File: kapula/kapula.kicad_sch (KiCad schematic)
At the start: 157 parts, among them J1 Conn_02x10_Odd_Even, J12 U.FL, J13 U.FL, J3 Conn_02x10_Odd_Even, J4 Conn_ARM_JTAG_SWD_10, J5 U.FL, J9 U.FL, Q1 AO3401A, Q1 BSS84, Q2 AO3401A, Q3 AO3400A, Q5 AO3400A, Q6 AO3400A, T1 BW21S7511A01TF, T2 BW21S7511A01TF, T3 BW21S7511A01TF, T4 BW21S7511A01TF, U1 XC6206P332MR, U2 TP4054, U3 DW01+G, U5 EFR32FG14P233F256GM48-B, U6 XA213-G4J, X1 DSB221SDN, Y1 32768 Hz

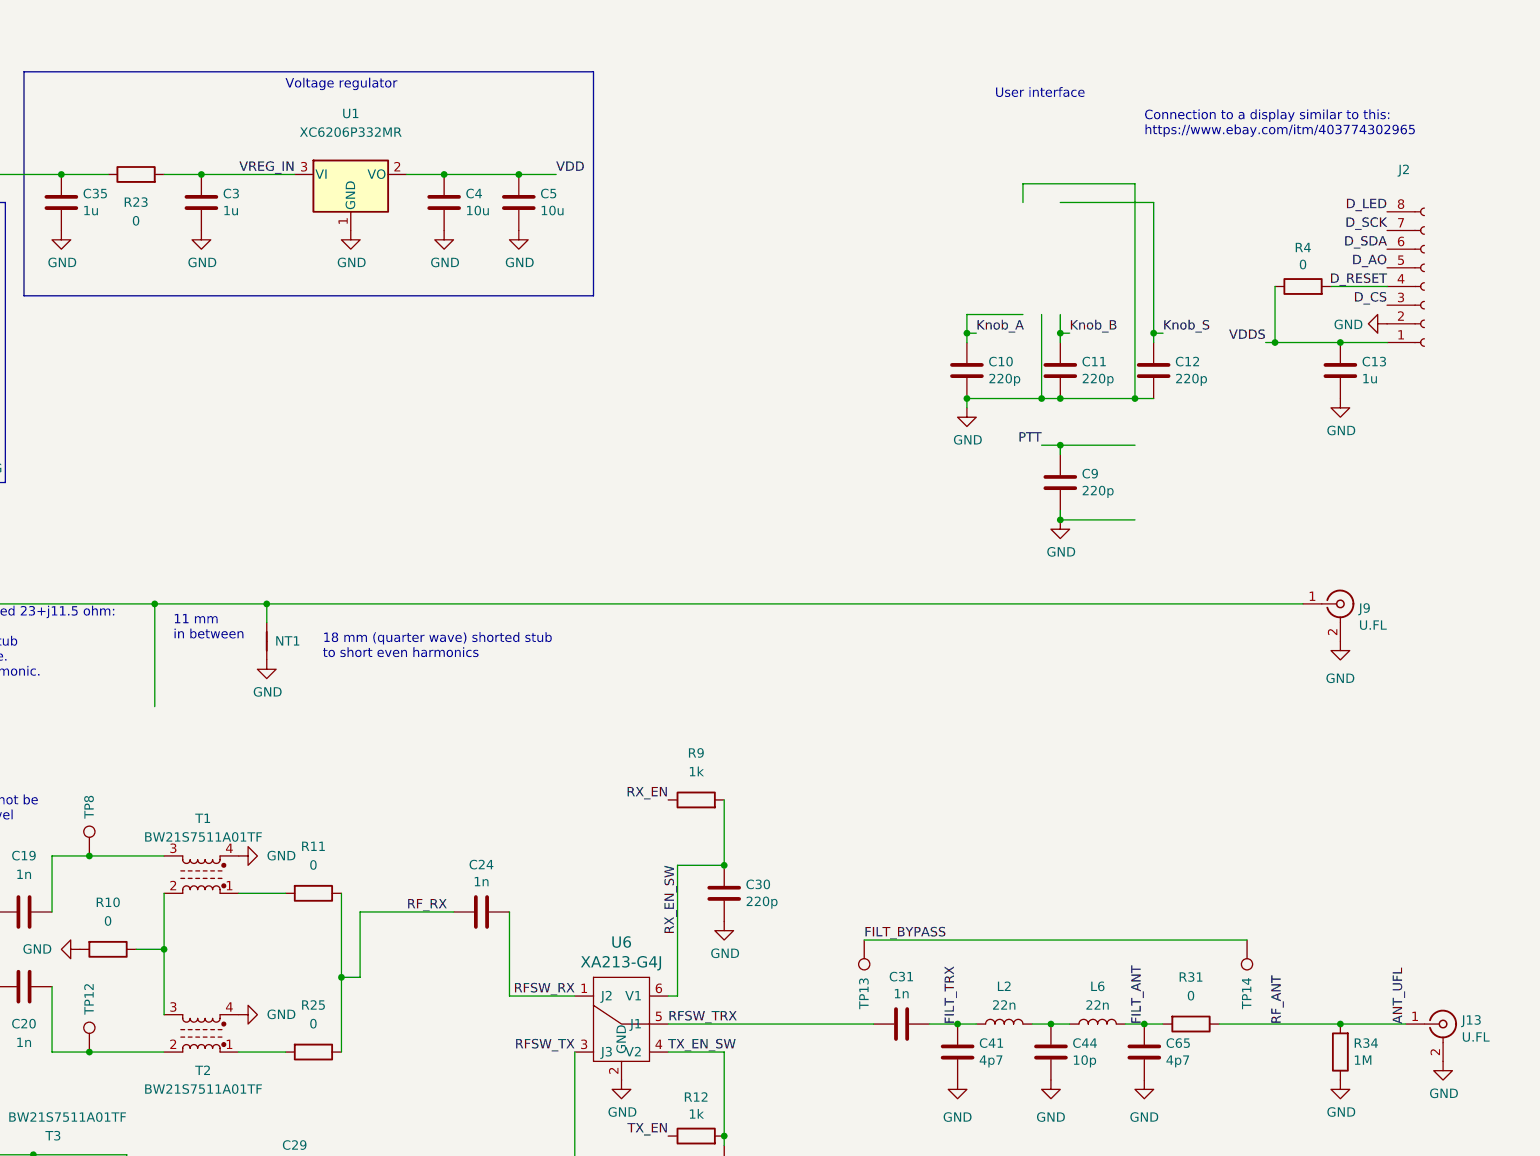
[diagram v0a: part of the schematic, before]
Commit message: PCB: Fix ERC errors
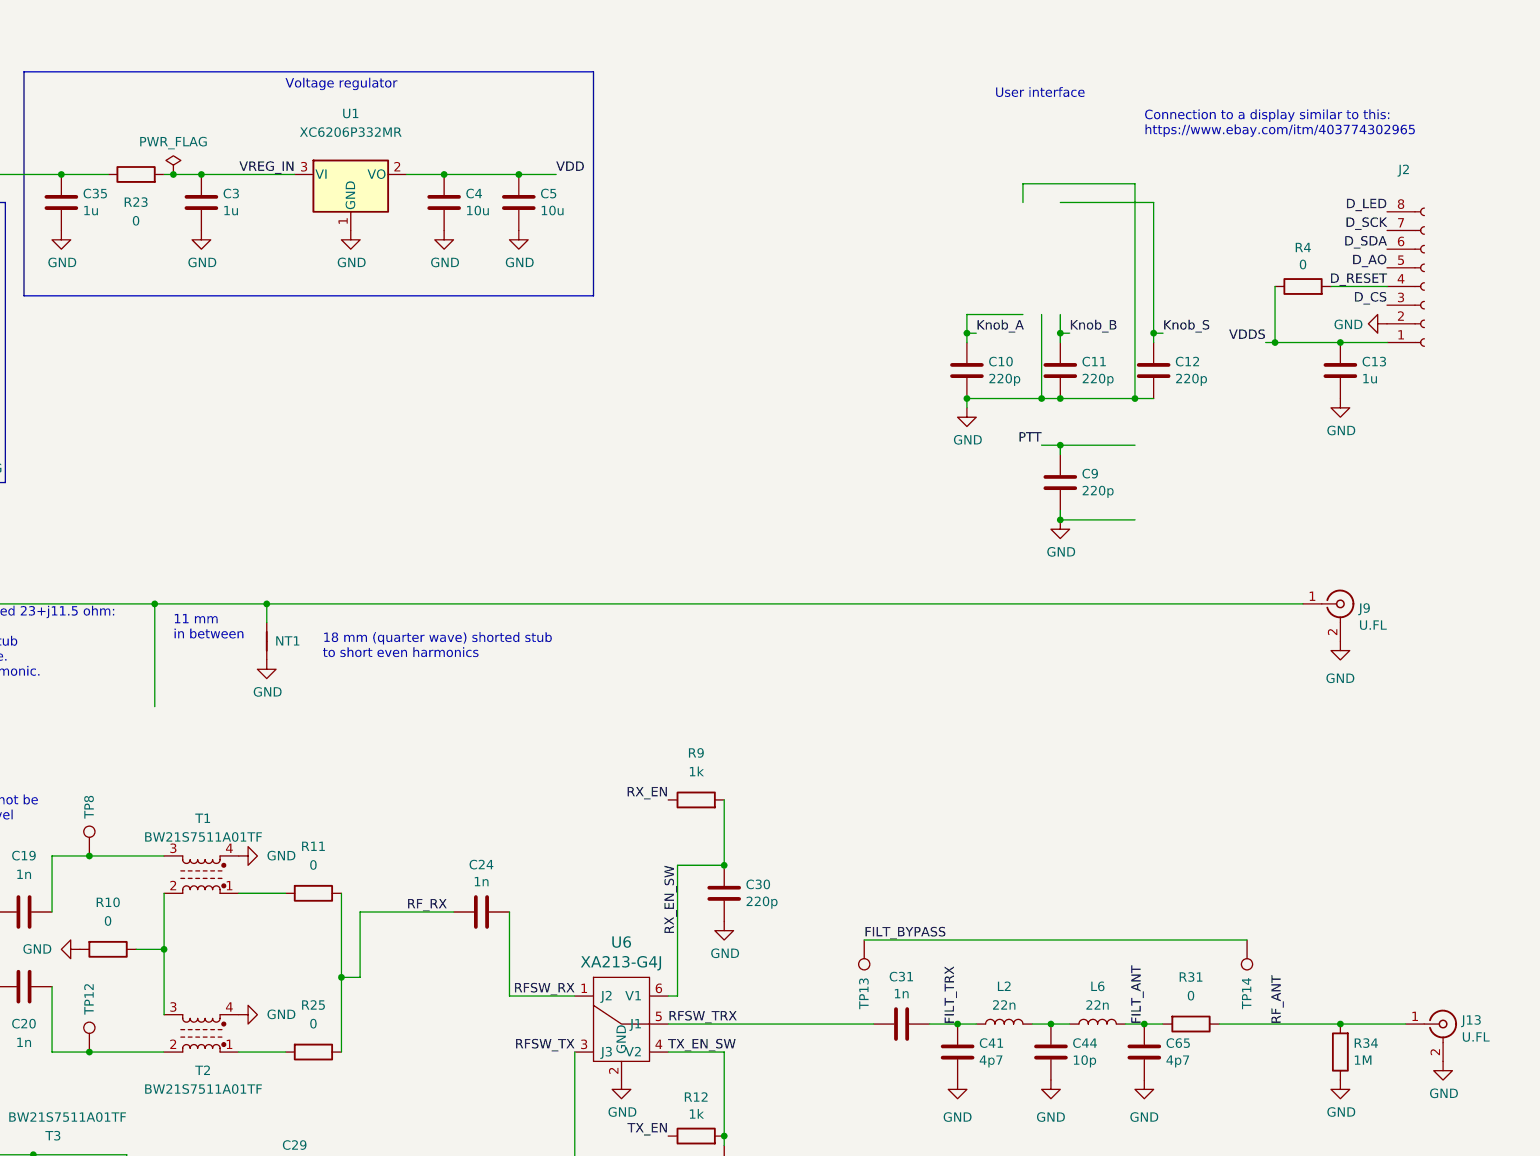
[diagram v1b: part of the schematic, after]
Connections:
- net ANT_UFL renamed RF_ANT
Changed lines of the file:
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@@
   (junction (at 219.71 261.62) (diameter 0) (color 0 0 0 0)
   )
+  (junction (at 232.41 26.67) (diameter 0) (color 0 0 0 0)
+  )
   (junction (at 53.34 119.38) (diameter 0) (color 0 0 0 0)
   )
@@
     (stroke (width 0) (type default))
   )
+  (wire (pts (xy 232.41 26.67) (xy 236.22 26.67))
+    (stroke (width 0) (type default))
+  )
   (polyline (pts (xy 298.45 215.9) (xy 298.45 280.67))
     (stroke (width 0) (type default))
@@
     (stroke (width 0) (type default))
   )
-  (wire (pts (xy 231.14 26.67) (xy 236.22 26.67))
+  (wire (pts (xy 231.14 26.67) (xy 232.41 26.67))
     (stroke (width 0) (type default))
   )
@@
     (effects (font (size 1.27 1.27)) (justify right bottom))
   )
-  (label "ANT_UFL" (at 400.05 142.24 90) (fields_autoplaced)
-    (effects (font (size 1.27 1.27)) (justify left bottom))
-  )
   (label "Knob_S" (at 328.93 177.8 180) (fields_autoplaced)
     (effects (font (size 1.27 1.27)) (justify right bottom))
@@
         )
       )
+    )
+  )
+  (symbol (lib_id "power:PWR_FLAG") (at 232.41 26.67 0) (unit 1)
+    (in_bom yes) (on_board yes) (dnp no)
+    (property "Reference" "#FLG09" (at 232.41 24.765 0)
+      (effects (font (size 1.27 1.27)) hide)
+    )
+    (property "Value" "PWR_FLAG" (at 232.41 22.2504 0)
+      (effects (font (size 1.27 1.27)))
+    )
+    (property "Footprint" "" (at 232.41 26.67 0)
+      (effects (font (size 1.27 1.27)) hide)
+    )
+    (property "Datasheet" "~" (at 232.41 26.67 0)
+      (effects (font (size 1.27 1.27)) hide)
+    )
+    (pin "1")
+    (instances
+      (project "kapula"
+        (path "/f2315993-072e-45c9-8c85-e79c6d40aba4"
+          (reference "#FLG09") (unit 1)
+        )
+      )

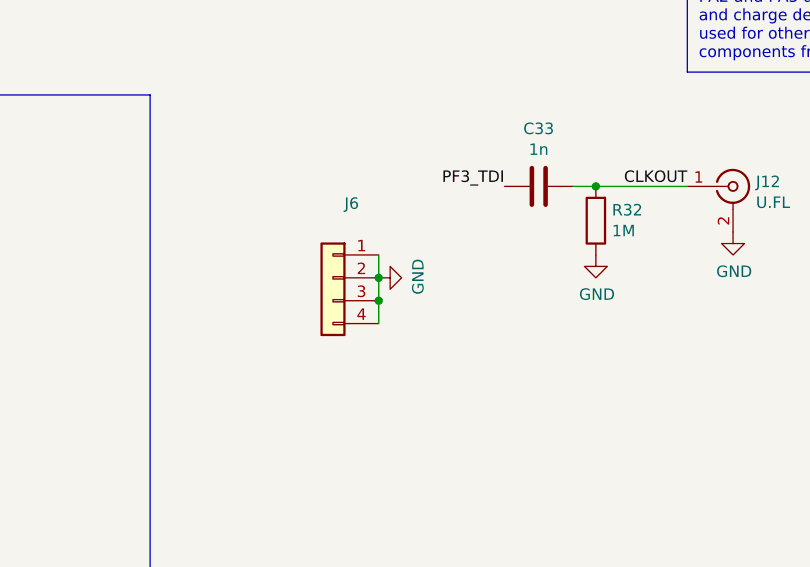
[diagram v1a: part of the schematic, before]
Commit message: PCB: Add 0-ohm resistors for extra ground header
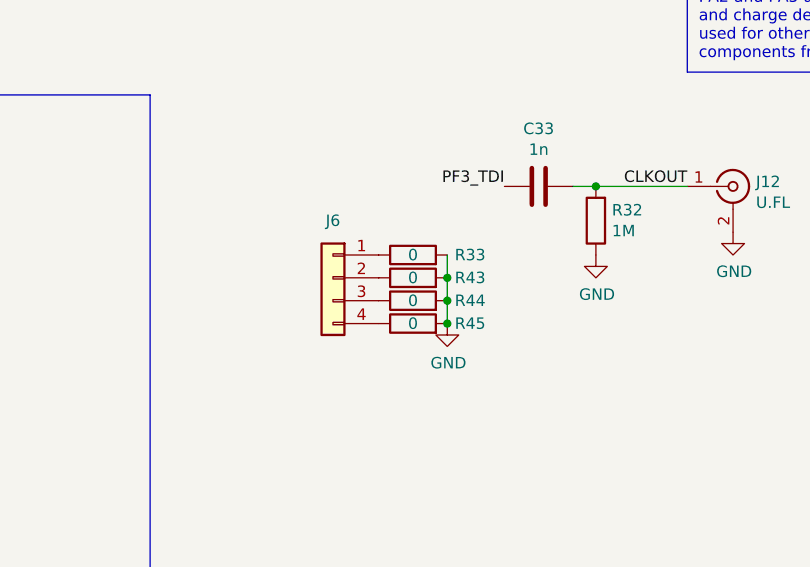
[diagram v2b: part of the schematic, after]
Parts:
- added R33, R43, R44, R45: 0, kapula:R_0402_to_0603_HandSolder, symbol Device:R
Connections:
- net GND: now also R33.2, R43.2, R44.2, R45.2; no longer J6.1 (Pin_1), J6.2 (Pin_2), J6.3 (Pin_3), J6.4 (Pin_4)
- new net: J6.1 (Pin_1), R33.1
- new net: J6.2 (Pin_2), R43.1
- new net: J6.3 (Pin_3), R44.1
- new net: J6.4 (Pin_4), R45.1
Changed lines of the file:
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@@
   (junction (at 217.17 26.67) (diameter 0) (color 0 0 0 0)
   )
+  (junction (at 331.47 236.22) (diameter 0) (color 0 0 0 0)
+  )
   (junction (at 74.93 121.92) (diameter 0) (color 0 0 0 0)
   )
@@
   (junction (at 95.25 99.06) (diameter 0) (color 0 0 0 0)
   )
-  (junction (at 323.85 236.22) (diameter 0) (color 0 0 0 0)
-  )
   (junction (at 185.42 127) (diameter 0) (color 0 0 0 0)
   )
@@
   (junction (at 66.04 26.67) (diameter 0) (color 0 0 0 0)
   )
+  (junction (at 331.47 238.76) (diameter 0) (color 0 0 0 0)
+  )
   (junction (at 236.22 26.67) (diameter 0) (color 0 0 0 0)
   )
@@
   (junction (at 69.85 231.14) (diameter 0) (color 0 0 0 0)
   )
-  (junction (at 323.85 238.76) (diameter 0) (color 0 0 0 0)
-  )
   (junction (at 340.36 48.26) (diameter 0) (color 0 0 0 0)
   )
@@
   (junction (at 43.18 119.38) (diameter 0) (color 0 0 0 0)
   )
+  (junction (at 331.47 241.3) (diameter 0) (color 0 0 0 0)
+  )
   (junction (at 307.34 120.65) (diameter 0) (color 0 0 0 0)
   )
@@
     (stroke (width 0) (type default))
   )
-  (wire (pts (xy 323.85 236.22) (xy 323.85 238.76))
-    (stroke (width 0) (type default))
-  )
   (wire (pts (xy 218.44 177.8) (xy 226.06 177.8))
     (stroke (width 0) (type default))
@@
     (stroke (width 0) (type default))
   )
+  (wire (pts (xy 331.47 236.22) (xy 331.47 238.76))
+    (stroke (width 0) (type default))
+  )
   (wire (pts (xy 381 49.53) (xy 382.27 49.53))
     (stroke (width 0) (type default))
@@
     (stroke (width 0) (type default))
   )
+  (wire (pts (xy 331.47 238.76) (xy 331.47 241.3))
+    (stroke (width 0) (type default))
+  )
   (wire (pts (xy 86.36 124.46) (xy 110.49 124.46))
     (stroke (width 0) (type default))
@@
     (stroke (width 0) (type default))
   )
-  (wire (pts (xy 323.85 233.68) (xy 323.85 236.22))
-    (stroke (width 0) (type default))
-  )
   (wire (pts (xy 238.76 233.68) (xy 252.73 233.68))
     (stroke (width 0) (type default))
@@
     (stroke (width 0) (type default))
   )
+  (wire (pts (xy 331.47 233.68) (xy 331.47 236.22))
+    (stroke (width 0) (type default))
+  )
   (wire (pts (xy 241.3 146.05) (xy 247.65 146.05))
     (stroke (width 0) (type default))
@@
     (stroke (width 0) (type default))
   )
-  (wire (pts (xy 323.85 238.76) (xy 323.85 241.3))
-    (stroke (width 0) (type default))
-  )
   (polyline (pts (xy 143.51 215.9) (xy 298.45 215.9))
     (stroke (width 0) (type default))
@@
   )
   (symbol (lib_id "Connector_Generic:Conn_01x04") (at 318.77 236.22 0) (mirror y) (unit 1)
-    (in_bom yes) (on_board yes) (dnp no)
-    (property "Reference" "J6" (at 320.8528 227.965 0)
+    (in_bom yes) (on_board yes) (dnp no) (fields_autoplaced)
+    (property "Reference" "J6" (at 318.77 229.87 0)
       (effects (font (size 1.27 1.27)))
     )
@@
     )
   )
-  (symbol (lib_id "power:GND") (at 323.85 236.22 90) (unit 1)
-    (in_bom yes) (on_board yes) (dnp no)
-    (property "Reference" "#PWR058" (at 330.2 236.22 0)
-      (effects (font (size 1.27 1.27)) hide)
-    )
-    (property "Value" "GND" (at 328.2442 236.093 0)
-      (effects (font (size 1.27 1.27)))
-    )
-    (property "Footprint" "" (at 323.85 236.22 0)
-      (effects (font (size 1.27 1.27)) hide)
-    )
-    (property "Datasheet" "" (at 323.85 236.22 0)
-      (effects (font (size 1.27 1.27)) hide)
-    )
-    (pin "1")
-    (instances
-      (project "kapula"
-        (path "/f2315993-072e-45c9-8c85-e79c6d40aba4"
-          (reference "#PWR058") (unit 1)
-        )
-      )
-    )
-  )
   (symbol (lib_id "Device:R") (at 198.12 -43.18 180) (unit 1)
     (in_bom yes) (on_board yes) (dnp no)
@@
     )
   )
+  (symbol (lib_id "Device:R") (at 327.66 233.68 90) (unit 1)
+    (in_bom yes) (on_board yes) (dnp no)
+    (property "Reference" "R33" (at 334.01 233.68 90)
+      (effects (font (size 1.27 1.27)))
+    )
+    (property "Value" "0" (at 327.66 233.68 90)
+      (effects (font (size 1.27 1.27)))
+    )
+    (property "Footprint" "kapula:R_0402_to_0603_HandSolder" (at 327.66 235.458 90)
+      (effects (font (size 1.27 1.27)) hide)
+    )
+    (property "Datasheet" "" (at 327.66 233.68 0)
+      (effects (font (size 1.27 1.27)) hide)
+    )
+    (property "LCSC" "C17168" (at 327.66 233.68 0)
+      (effects (font (size 1.27 1.27)) hide)
+    )
+    (pin "1")
+    (pin "2")
+    (instances
+      (project "kapula"
+        (path "/f2315993-072e-45c9-8c85-e79c6d40aba4"
+          (reference "R33") (unit 1)
+        )
+      )
+    )
+  )
   (symbol (lib_id "Device:R") (at 96.52 35.56 180) (unit 1)
     (in_bom yes) (on_board yes) (dnp no) (fields_autoplaced)
@@
     )
   )
+  (symbol (lib_id "Device:R") (at 327.66 241.3 90) (unit 1)
+    (in_bom yes) (on_board yes) (dnp no)
+    (property "Reference" "R45" (at 334.01 241.3 90)
+      (effects (font (size 1.27 1.27)))
+    )
+    (property "Value" "0" (at 327.66 241.3 90)
+      (effects (font (size 1.27 1.27)))
+    )
+    (property "Footprint" "kapula:R_0402_to_0603_HandSolder" (at 327.66 243.078 90)
+      (effects (font (size 1.27 1.27)) hide)
+    )
+    (property "Datasheet" "" (at 327.66 241.3 0)
+      (effects (font (size 1.27 1.27)) hide)
+    )
+    (property "LCSC" "C17168" (at 327.66 241.3 0)
+      (effects (font (size 1.27 1.27)) hide)
+    )
+    (pin "1")
+    (pin "2")
+    (instances
+      (project "kapula"
+        (path "/f2315993-072e-45c9-8c85-e79c6d40aba4"
+          (reference "R45") (unit 1)
+        )
+      )
+    )
+  )
   (symbol (lib_id "power:GND") (at 341.63 198.12 90) (unit 1)
     (in_bom yes) (on_board yes) (dnp no) (fields_autoplaced)
@@
     )
   )
+  (symbol (lib_id "power:GND") (at 331.47 241.3 0) (unit 1)
+    (in_bom yes) (on_board yes) (dnp no)
+    (property "Reference" "#PWR058" (at 331.47 247.65 0)
+      (effects (font (size 1.27 1.27)) hide)
+    )
+    (property "Value" "GND" (at 331.597 245.6942 0)
+      (effects (font (size 1.27 1.27)))
+    )
+    (property "Footprint" "" (at 331.47 241.3 0)
+      (effects (font (size 1.27 1.27)) hide)
+    )
+    (property "Datasheet" "" (at 331.47 241.3 0)
+      (effects (font (size 1.27 1.27)) hide)
+    )
+    (pin "1")
+    (instances
+      (project "kapula"
+        (path "/f2315993-072e-45c9-8c85-e79c6d40aba4"
+          (reference "#PWR058") (unit 1)
+        )
+      )
+    )
+  )
   (symbol (lib_id "Device:R") (at 212.09 254 90) (unit 1)
     (in_bom yes) (on_board yes) (dnp no) (fields_autoplaced)
@@
     )
   )
+  (symbol (lib_id "Device:R") (at 327.66 238.76 90) (unit 1)
+    (in_bom yes) (on_board yes) (dnp no)
+    (property "Reference" "R44" (at 334.01 238.76 90)
+      (effects (font (size 1.27 1.27)))
+    )
+    (property "Value" "0" (at 327.66 238.76 90)
+      (effects (font (size 1.27 1.27)))
+    )
+    (property "Footprint" "kapula:R_0402_to_0603_HandSolder" (at 327.66 240.538 90)
+      (effects (font (size 1.27 1.27)) hide)
+    )
+    (property "Datasheet" "" (at 327.66 238.76 0)
+      (effects (font (size 1.27 1.27)) hide)
+    )
+    (property "LCSC" "C17168" (at 327.66 238.76 0)
+      (effects (font (size 1.27 1.27)) hide)
+    )
+    (pin "1")
+    (pin "2")
+    (instances
+      (project "kapula"
+        (path "/f2315993-072e-45c9-8c85-e79c6d40aba4"
+          (reference "R44") (unit 1)
+        )
+      )
+    )
+  )
   (symbol (lib_id "Device:L_Ferrite_Coupled_1243") (at 234.95 168.91 180) (unit 1)
     (in_bom yes) (on_board yes) (dnp no) (fields_autoplaced)
@@
         )
       )
+    )
+  )
+  (symbol (lib_id "Device:R") (at 327.66 236.22 90) (unit 1)
+    (in_bom yes) (on_board yes) (dnp no)
+    (property "Reference" "R43" (at 334.01 236.22 90)
+      (effects (font (size 1.27 1.27)))
+    )
+    (property "Value" "0" (at 327.66 236.22 90)
+      (effects (font (size 1.27 1.27)))
+    )
+    (property "Footprint" "kapula:R_0402_to_0603_HandSolder" (at 327.66 237.998 90)
+      (effects (font (size 1.27 1.27)) hide)
+    )
+    (property "Datasheet" "" (at 327.66 236.22 0)
+      (effects (font (size 1.27 1.27)) hide)
+    )
+    (property "LCSC" "C17168" (at 327.66 236.22 0)
+      (effects (font (size 1.27 1.27)) hide)
+    )
+    (pin "1")
+    (pin "2")
+    (instances
+      (project "kapula"
+        (path "/f2315993-072e-45c9-8c85-e79c6d40aba4"
+          (reference "R43") (unit 1)
+        )
+      )

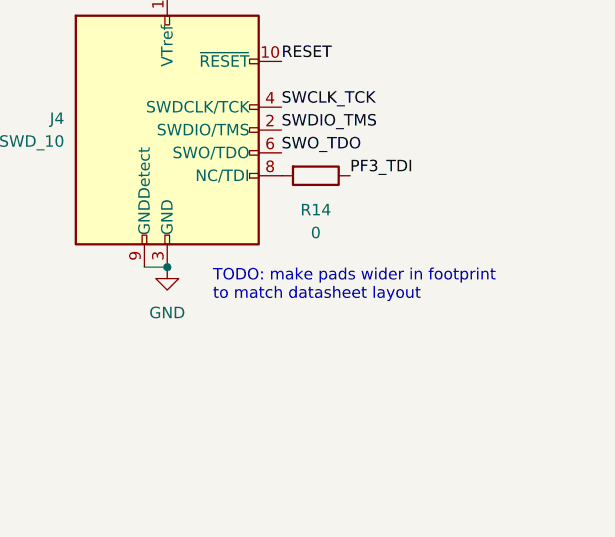
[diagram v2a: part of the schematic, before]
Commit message: PCB: Fix programming header footprint
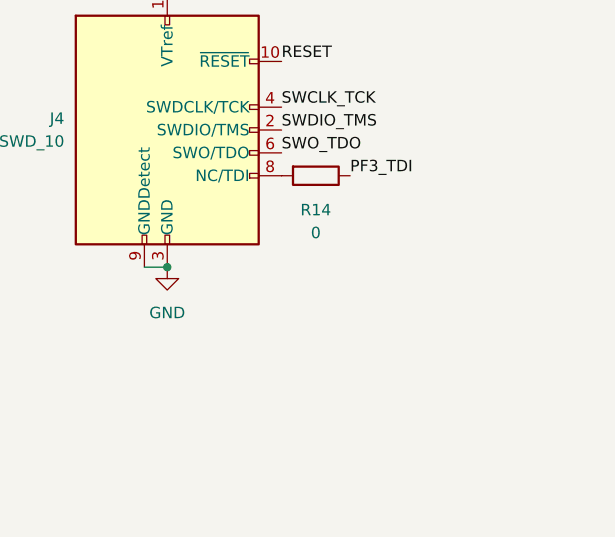
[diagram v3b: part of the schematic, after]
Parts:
- J4: footprint Connector_PinHeader_1.27mm:PinHeader_2x05_P1.27mm_Vertical_SMD -> kapula:DZ127S-22-10-55
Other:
- note removed: "TODO: make pads wider in footprint to match datasheet layout"
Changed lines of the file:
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@@
     (effects (font (size 1.27 1.27)) (justify left bottom))
   )
-  (text "TODO: make pads wider in footprint\nto match datasheet layout"
-    (at 444.5 256.54 0)
-    (effects (font (size 1.27 1.27)) (justify left bottom))
-  )
   (text "38.4 MHz TCXO" (at 116.84 215.9 0)
     (effects (font (size 1.27 1.27)) (justify left bottom))
@@
       (effects (font (size 1.27 1.27)) (justify right))
     )
-    (property "Footprint" "Connector_PinHeader_1.27mm:PinHeader_2x05_P1.27mm_Vertical_SMD" (at 439.42 237.49 0)
+    (property "Footprint" "kapula:DZ127S-22-10-55" (at 439.42 237.49 0)
       (effects (font (size 1.27 1.27)) hide)
     )
